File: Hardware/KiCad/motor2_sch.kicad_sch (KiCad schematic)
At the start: 5 parts, among them U102 TB6612FNG

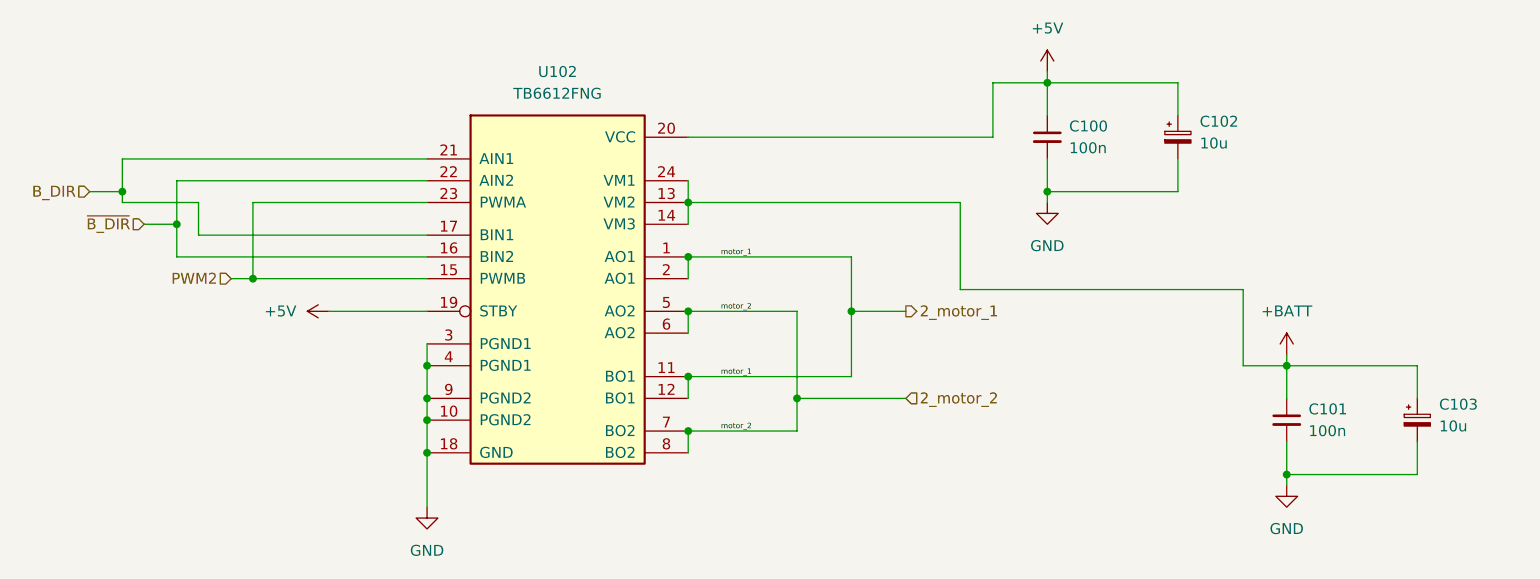
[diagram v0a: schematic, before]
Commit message: change to pinout of atemega for PWM Motor 1
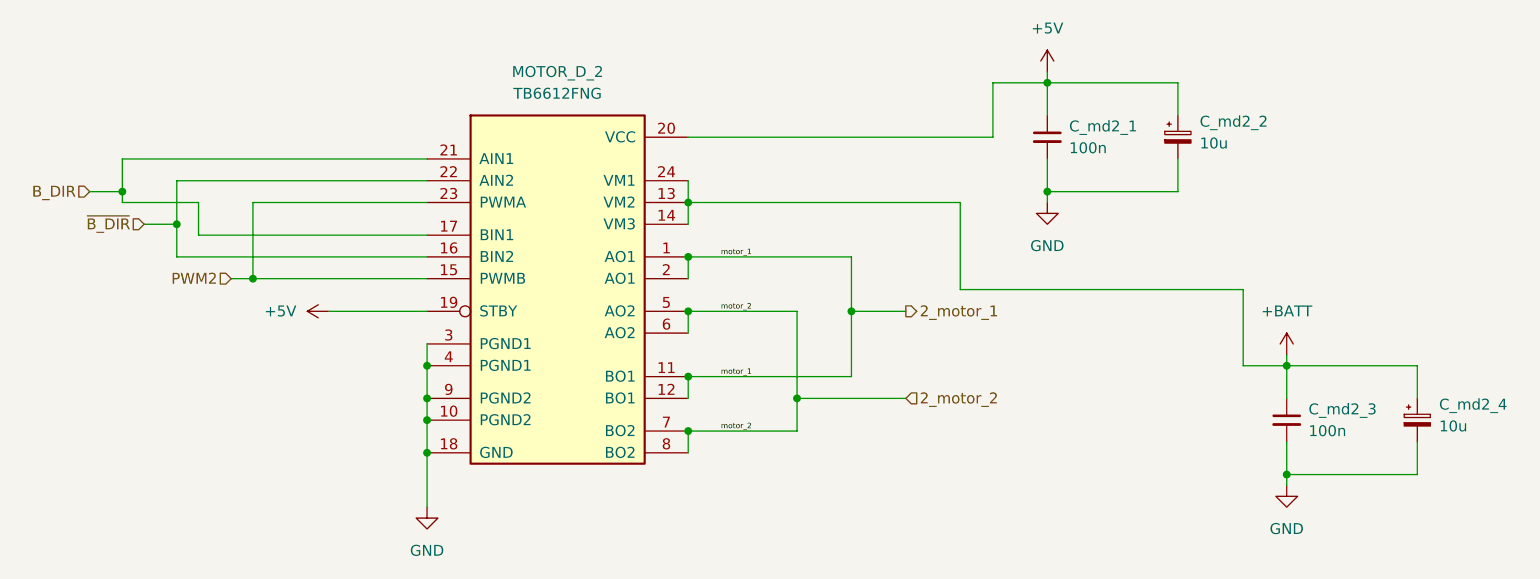
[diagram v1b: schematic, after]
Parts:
- renumbered C100 to C_md2_1, C102 to C_md2_2, C101 to C_md2_3, C103 to C_md2_4, U102 to MOTOR_D_2
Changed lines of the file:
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@@
 (kicad_sch
-	(version 20231120)
+	(version 20250114)
 	(generator "eeschema")
-	(generator_version "8.0")
+	(generator_version "9.0")
 	(paper "A4")
 	(junction
@@
 	(label "motor_1"
 		(at 118.11 59.69 0)
-		(fields_autoplaced yes)
 		(effects
 			(font
@@
 	(label "motor_1"
 		(at 118.11 73.66 0)
-		(fields_autoplaced yes)
 		(effects
 			(font
@@
 	(label "motor_2"
 		(at 118.11 66.04 0)
-		(fields_autoplaced yes)
 		(effects
 			(font
@@
 	(label "motor_2"
 		(at 118.11 80.01 0)
-		(fields_autoplaced yes)
 		(effects
 			(font
@@
 		(shape input)
 		(at 139.7 76.2 0)
-		(fields_autoplaced yes)
 		(effects
 			(font
@@
 		(shape input)
 		(at 50.8 55.88 180)
-		(fields_autoplaced yes)
 		(effects
 			(font
@@
 		(shape input)
 		(at 44.45 52.07 180)
-		(fields_autoplaced yes)
 		(effects
 			(font
@@
 		(shape output)
 		(at 139.7 66.04 0)
-		(fields_autoplaced yes)
 		(effects
 			(font
@@
 		(shape input)
 		(at 60.96 62.23 180)
-		(fields_autoplaced yes)
 		(effects
 			(font
@@
 		(dnp no)
 		(fields_autoplaced yes)
-		(property "Reference" "C103"
+		(property "Reference" "C_md2_4"
 			(at 201.93 76.9238 0)
 			(effects
@@
 		(dnp no)
 		(fields_autoplaced yes)
-		(property "Reference" "#PWR0115"
+		(property "Reference" "#PWR019"
 			(at 184.15 74.93 0)
 			(effects
@@
 		(dnp no)
 		(fields_autoplaced yes)
-		(property "Reference" "C101"
+		(property "Reference" "C_md2_3"
 			(at 186.69 77.4762 0)
 			(effects
@@
 		(dnp no)
 		(fields_autoplaced yes)
-		(property "Reference" "U102"
+		(property "Reference" "MOTOR_D_2"
 			(at 99.06 38.1 0)
 			(effects
@@
 		(dnp no)
 		(fields_autoplaced yes)
-		(property "Reference" "#PWR0114"
+		(property "Reference" "#PWR018"
 			(at 156.21 59.69 0)
 			(effects
@@
 		(dnp no)
 		(fields_autoplaced yes)
-		(property "Reference" "C102"
+		(property "Reference" "C_md2_2"
 			(at 173.99 43.9038 0)
 			(effects
@@
 		(dnp no)
 		(fields_autoplaced yes)
-		(property "Reference" "#PWR0103"
+		(property "Reference" "#PWR015"
 			(at 76.2 66.04 0)
 			(effects
@@
 		(dnp no)
 		(fields_autoplaced yes)
-		(property "Reference" "C100"
+		(property "Reference" "C_md2_1"
 			(at 158.75 44.4562 0)
 			(effects
@@
 		(dnp no)
 		(fields_autoplaced yes)
-		(property "Reference" "#PWR0113"
+		(property "Reference" "#PWR017"
 			(at 156.21 41.91 0)
 			(effects
@@
 		(dnp no)
 		(fields_autoplaced yes)
-		(property "Reference" "#PWR0118"
+		(property "Reference" "#PWR020"
 			(at 184.15 92.71 0)
 			(effects
@@
 		(dnp no)
 		(fields_autoplaced yes)
-		(property "Reference" "#PWR0104"
+		(property "Reference" "#PWR016"
 			(at 83.82 95.25 0)
 			(effects
